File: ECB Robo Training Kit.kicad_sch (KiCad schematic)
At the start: 43 parts, among them J1 Ultrsonic, J2 Barrel_Jack_Switch, J3 LCD, J4 DC Motor, K1 Relay SPDT, M1 Servo Motor, Q1 BC547, Q2 BC547, SW1 Switch 1, SW2 Switch 2, SW3 Switch 3, U1 DHT22, U2 HALL EFFECT, U3 IR, U4 L293D

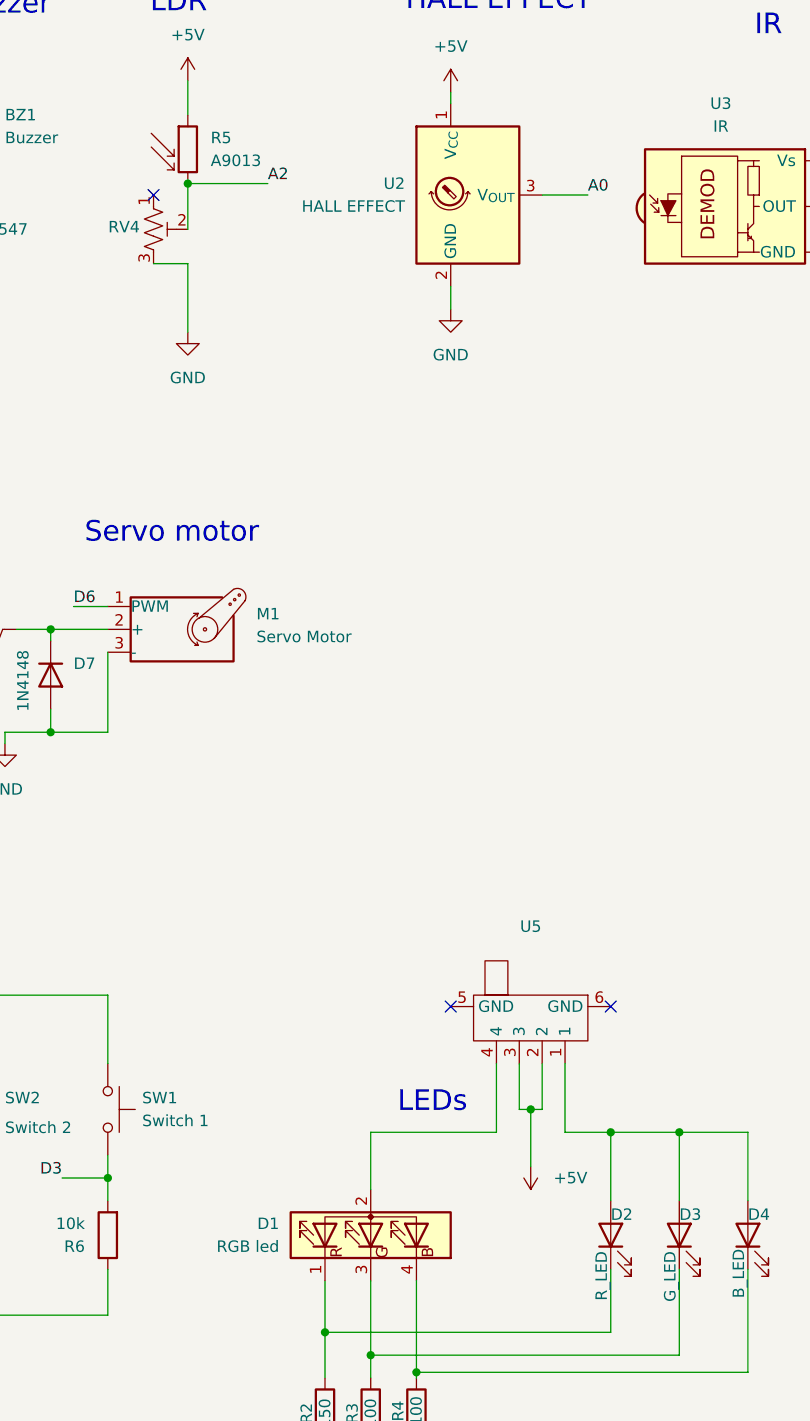
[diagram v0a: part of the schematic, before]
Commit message: Changed the silkscreen and pin a0 and a2. Added 3d models in the PCB
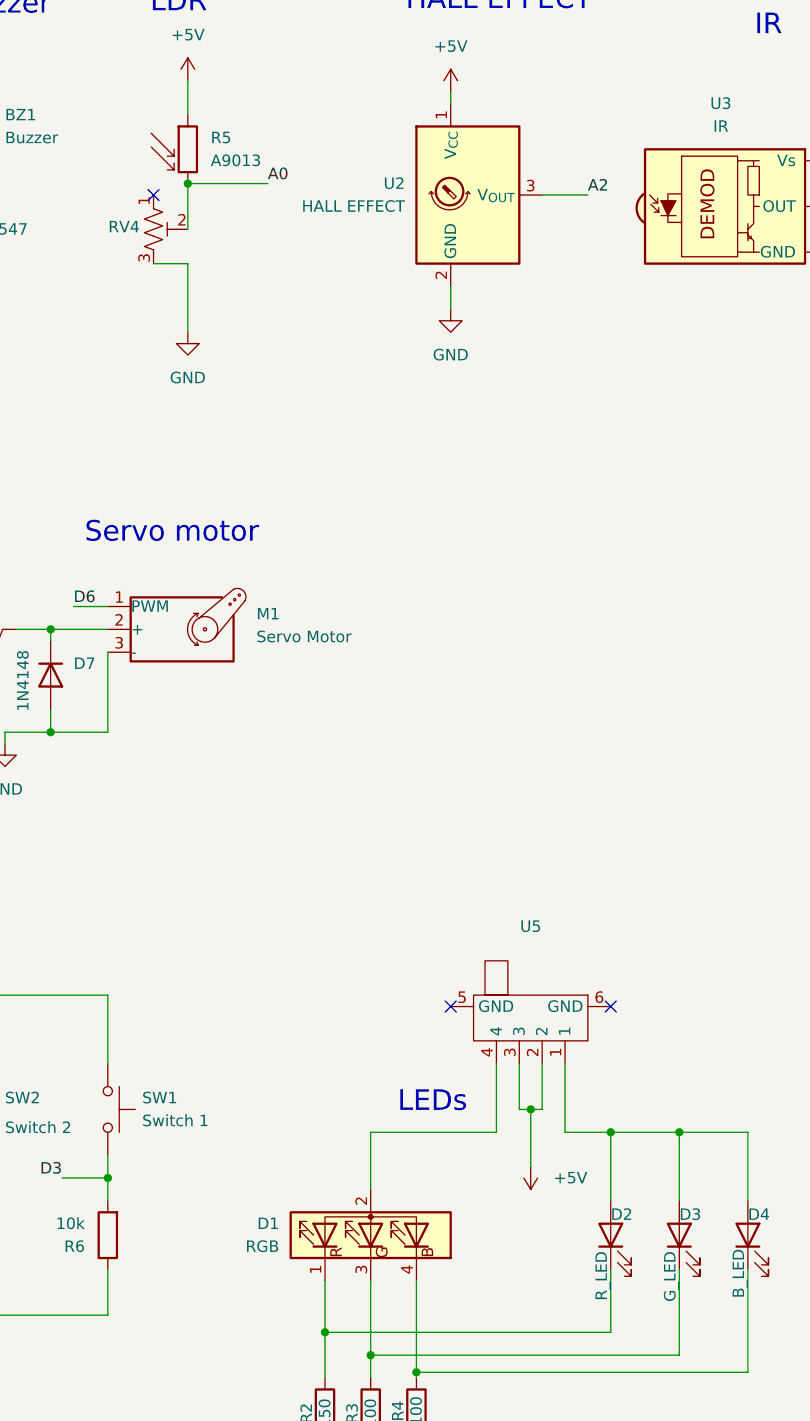
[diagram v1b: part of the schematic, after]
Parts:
- D1: value RGB led -> RGB
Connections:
- net A0: now also R5.2, RV4.2; no longer U2.3 (V_{OUT})
- net A2: now also U2.3 (V_{OUT}); no longer R5.2, RV4.2
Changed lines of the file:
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@@
 				)
 			)
-			(table_cell "Hall Effect"
+			(table_cell "LDR"
 				(exclude_from_sim no)
 				(at 199.39 134.62 0)
@@
 				)
 			)
-			(table_cell "LDR"
+			(table_cell "Hall Effect"
 				(exclude_from_sim no)
 				(at 199.39 139.7 0)
@@
 		)
 	)
-	(label "A0"
+	(label "A2"
 		(at 154.94 44.45 0)
 		(effects
@@
 		)
 	)
-	(label "A2"
+	(label "A0"
 		(at 119.38 43.18 0)
 		(effects
@@
 		)
 		(property "Description" "Generic connector, single row, 01x04, script generated"
-			(at 55.88 110.49 0)
+			(at 64.008 122.936 0)
 			(effects
 				(font
@@
 			)
 		)
-		(property "Value" "RGB led"
+		(property "Value" "RGB"
 			(at 120.65 161.2899 90)
 			(effects
